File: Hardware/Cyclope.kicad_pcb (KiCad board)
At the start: 2 copper layers, 30 x 80 mm, 75 parts, among them J1 M20-9762042, J2 Motor_2, J3 Motor_1, J4 Front, J5 Front, J8 FTDI, M1 FS5113R, M2 FS5113R, Q1 DMG3414U, Q2 DMG2301L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

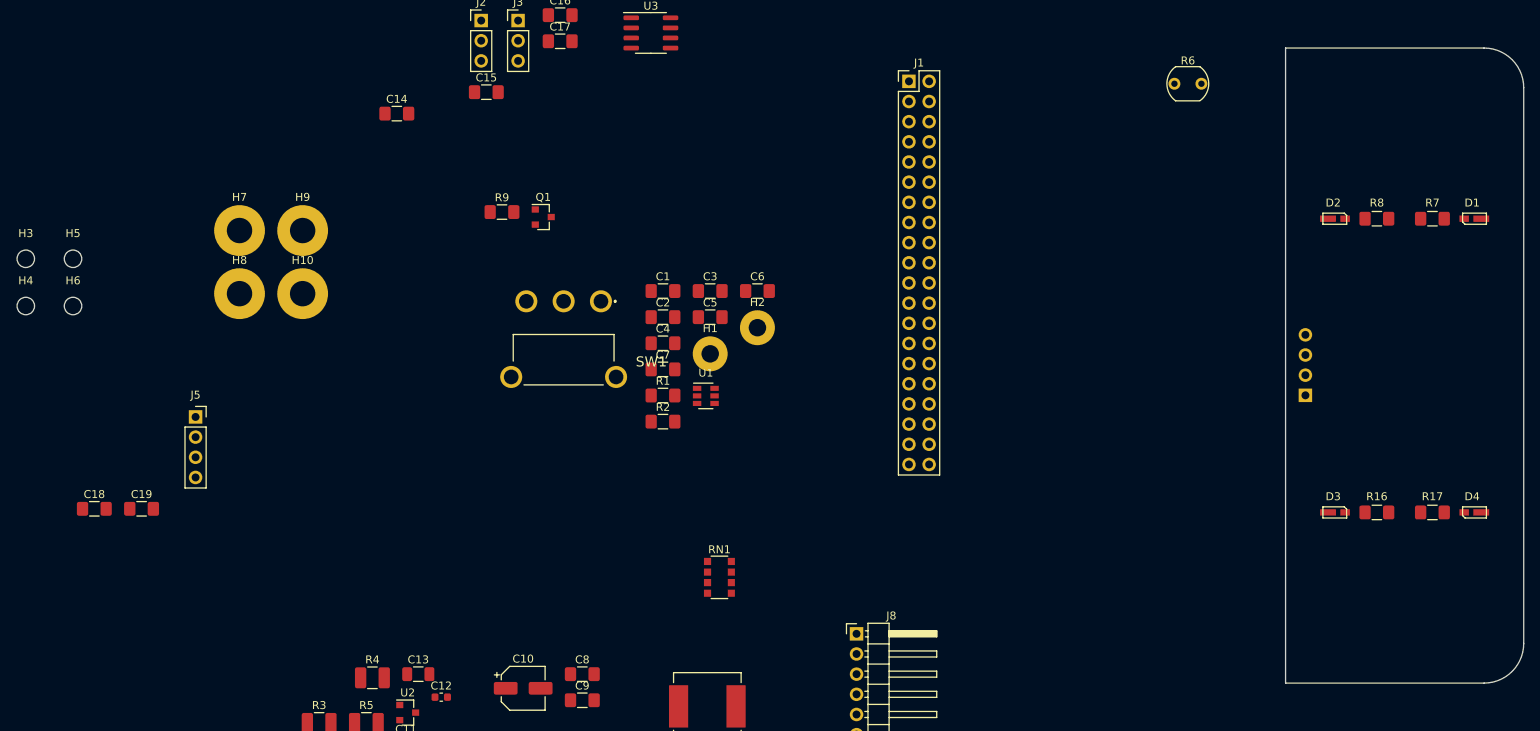
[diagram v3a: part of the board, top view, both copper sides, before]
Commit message: [Hardware] Added camera holes and a cut for camera cable to front board PCB.
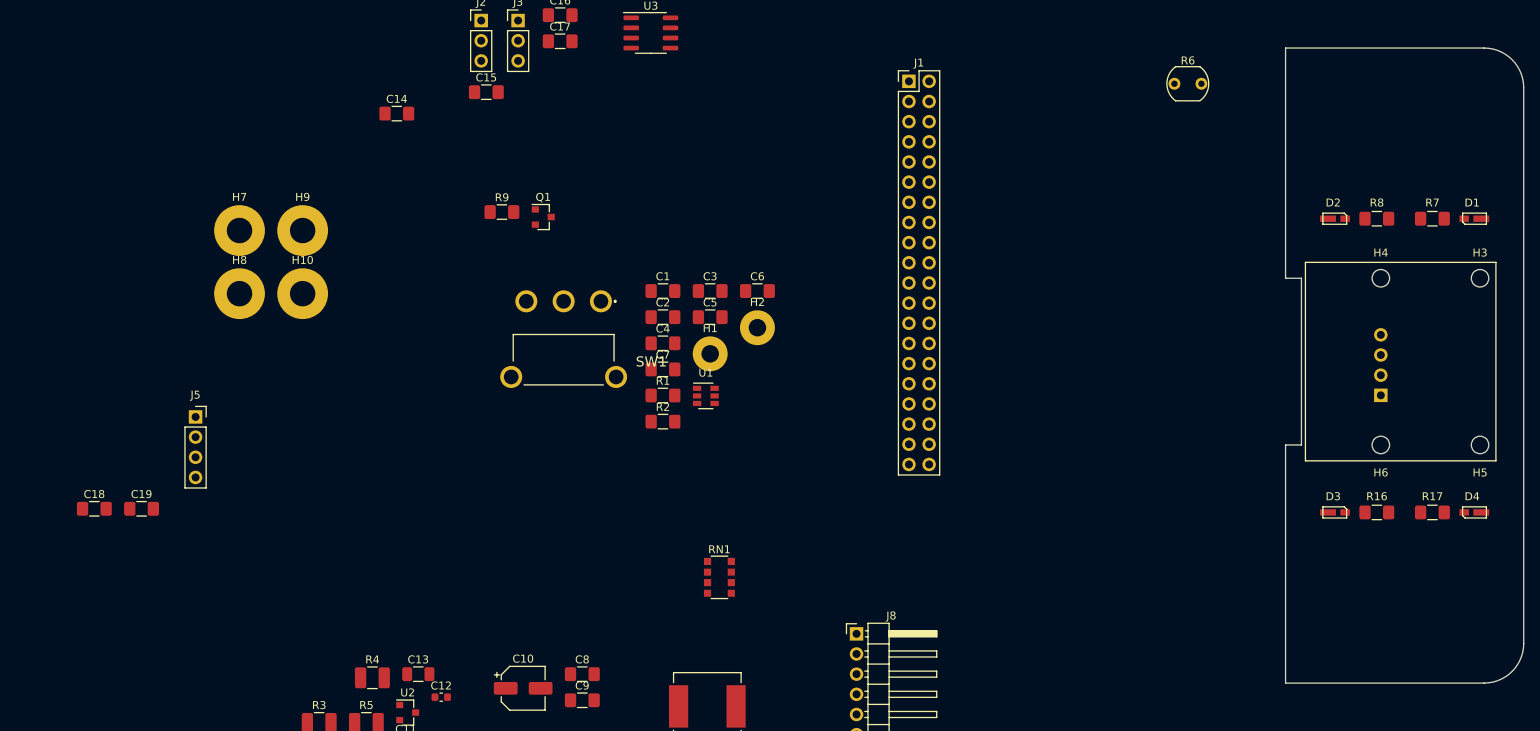
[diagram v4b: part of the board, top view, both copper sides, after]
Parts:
- moved H3 183.2 mm to (234.5, 69.0)
- moved H5 178.8 mm to (234.5, 90.0)
- moved H4 170.7 mm to (222.0, 69.0)
- moved H6 165.7 mm to (222.0, 90.0)
- moved J4 9.50 mm to (222.0, 83.8)
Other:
- outline, holes or cut-outs redrawn
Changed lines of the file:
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@@
   (general
     (thickness 1.6)
-    (drawings 14)
+    (drawings 22)
     (tracks 0)
     (zones 0)
@@
   )
   (module Connector_PinHeader_2.54mm:PinHeader_1x04_P2.54mm_Vertical (layer B.Cu)
-    (at 212.5 83.75)
+    (at 222 83.75)
     (descr "Through hole straight pin header, 1x04, 2.54mm pitch, single row")
     (tags "Through hole pin header THT 1x04 2.54mm single row")
-    (fp_text reference J4 (at 0 2.33) (layer B.SilkS)
+    (fp_text reference J4 (at 0 -10.25) (layer B.SilkS)
       (effects (font (size 1 1) (thickness 0.15)) (justify mirror))
     )
@@
   )
   (module MountingHole:MountingHole_2.2mm_M2 (layer F.Cu)
-    (at 57.258 72.498)
+    (at 222 90)
     (descr "Mounting Hole 2.2mm, no annular, M2")
     (tags "mounting hole 2.2mm no annular m2")
     (attr virtual)
-    (fp_text reference H6 (at 0 -3.2) (layer F.SilkS)
+    (fp_text reference H6 (at 0 3.5) (layer F.SilkS)
       (effects (font (size 1 1) (thickness 0.15)))
     )
@@
   )
   (module MountingHole:MountingHole_2.2mm_M2 (layer F.Cu)
-    (at 57.258 66.548)
+    (at 234.5 90)
     (descr "Mounting Hole 2.2mm, no annular, M2")
     (tags "mounting hole 2.2mm no annular m2")
     (attr virtual)
-    (fp_text reference H5 (at 0 -3.2) (layer F.SilkS)
+    (fp_text reference H5 (at 0 3.5) (layer F.SilkS)
       (effects (font (size 1 1) (thickness 0.15)))
     )
@@
   )
   (module MountingHole:MountingHole_2.2mm_M2 (layer F.Cu)
-    (at 51.308 72.498)
+    (at 222 69)
     (descr "Mounting Hole 2.2mm, no annular, M2")
     (tags "mounting hole 2.2mm no annular m2")
@@
   )
   (module MountingHole:MountingHole_2.2mm_M2 (layer F.Cu)
-    (at 51.308 66.548)
+    (at 234.5 69)
     (descr "Mounting Hole 2.2mm, no annular, M2")
     (tags "mounting hole 2.2mm no annular m2")
@@
     )
   )
-  (dimension 13 (width 0.15) (layer Dwgs.User)
-    (gr_text "13,000 mm" (at 194.2 68 270) (layer Dwgs.User)
-      (effects (font (size 1 1) (thickness 0.15)))
-    )
-    (feature1 (pts (xy 210 74.5) (xy 194.913579 74.5)))
-    (feature2 (pts (xy 210 61.5) (xy 194.913579 61.5)))
-    (crossbar (pts (xy 195.5 61.5) (xy 195.5 74.5)))
-    (arrow1a (pts (xy 195.5 74.5) (xy 194.913579 73.373496)))
-    (arrow1b (pts (xy 195.5 74.5) (xy 196.086421 73.373496)))
-    (arrow2a (pts (xy 195.5 61.5) (xy 194.913579 62.626504)))
-    (arrow2b (pts (xy 195.5 61.5) (xy 196.086421 62.626504)))
-  )
-  (dimension 13 (width 0.15) (layer Dwgs.User)
-    (gr_text "13,000 mm" (at 194.2 92 90) (layer Dwgs.User)
-      (effects (font (size 1 1) (thickness 0.15)))
-    )
-    (feature1 (pts (xy 210 85.5) (xy 194.913579 85.5)))
-    (feature2 (pts (xy 210 98.5) (xy 194.913579 98.5)))
-    (crossbar (pts (xy 195.5 98.5) (xy 195.5 85.5)))
-    (arrow1a (pts (xy 195.5 85.5) (xy 196.086421 86.626504)))
-    (arrow1b (pts (xy 195.5 85.5) (xy 194.913579 86.626504)))
-    (arrow2a (pts (xy 195.5 98.5) (xy 196.086421 97.373496)))
-    (arrow2b (pts (xy 195.5 98.5) (xy 194.913579 97.373496)))
-  )
-  (gr_arc (start 235 45) (end 240 45) (angle -90) (layer Edge.Cuts) (width 0.05))
-  (gr_arc (start 235 115) (end 235 120) (angle -90) (layer Edge.Cuts) (width 0.05))
+  (gr_line (start 210 90) (end 210 120) (layer Edge.Cuts) (width 0.1))
+  (gr_line (start 212 90) (end 210 90) (layer Edge.Cuts) (width 0.05))
+  (gr_line (start 212 69) (end 212 90) (layer Edge.Cuts) (width 0.1))
+  (gr_line (start 210 69) (end 212 69) (layer Edge.Cuts) (width 0.1))
+  (gr_line (start 212.5 92) (end 212.5 67) (layer F.SilkS) (width 0.15))
+  (gr_line (start 236.5 92) (end 212.5 92) (layer F.SilkS) (width 0.15))
+  (gr_line (start 236.5 67) (end 236.5 92) (layer F.SilkS) (width 0.15))
+  (gr_line (start 212.5 67) (end 236.5 67) (layer F.SilkS) (width 0.15))
+  (dimension 12.5 (width 0.15) (layer Dwgs.User)
+    (gr_text "12,500 mm" (at 228.25 129.3) (layer Dwgs.User)
+      (effects (font (size 1 1) (thickness 0.15)))
+    )
+    (feature1 (pts (xy 222 89.5) (xy 222 128.586421)))
+    (feature2 (pts (xy 234.5 89.5) (xy 234.5 128.586421)))
+    (crossbar (pts (xy 234.5 128) (xy 222 128)))
+    (arrow1a (pts (xy 222 128) (xy 223.126504 127.413579)))
+    (arrow1b (pts (xy 222 128) (xy 223.126504 128.586421)))
+    (arrow2a (pts (xy 234.5 128) (xy 233.373496 127.413579)))
+    (arrow2b (pts (xy 234.5 128) (xy 233.373496 128.586421)))
+  )
+  (dimension 21 (width 0.15) (layer Dwgs.User)
+    (gr_text "21,000 mm" (at 248.3 79.5 270) (layer Dwgs.User)
+      (effects (font (size 1 1) (thickness 0.15)))
+    )
+    (feature1 (pts (xy 217.5 90) (xy 247.586421 90)))
+    (feature2 (pts (xy 217.5 69) (xy 247.586421 69)))
+    (crossbar (pts (xy 247 69) (xy 247 90)))
+    (arrow1a (pts (xy 247 90) (xy 246.413579 88.873496)))
+    (arrow1b (pts (xy 247 90) (xy 247.586421 88.873496)))
+    (arrow2a (pts (xy 247 69) (xy 246.413579 70.126504)))
+    (arrow2b (pts (xy 247 69) (xy 247.586421 70.126504)))
+  )
+  (gr_arc (start 235 45) (end 240 45) (angle -90) (layer Edge.Cuts) (width 0.1))
+  (gr_arc (start 235 115) (end 235 120) (angle -90) (layer Edge.Cuts) (width 0.1))
   (dimension 16 (width 0.15) (layer Dwgs.User)
     (gr_text "16,000 mm" (at 252.3 112 270) (layer Dwgs.User)
@@
   (gr_line (start 240 45) (end 240 115) (layer Edge.Cuts) (width 0.1))
   (gr_line (start 210 40) (end 235 40) (layer Edge.Cuts) (width 0.1))
-  (gr_line (start 210 120) (end 210 40) (layer Edge.Cuts) (width 0.1))
+  (gr_line (start 210 69) (end 210 40) (layer Edge.Cuts) (width 0.1))
   (gr_line (start 235 120) (end 210 120) (layer Edge.Cuts) (width 0.1))
   (gr_text GND (at 169.164 113.792) (layer F.Mask)

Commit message: [Hardware] Positionned LDR on front board PCB.
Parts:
- moved R6 82.8 mm to (236.0, 117.0), turned to 90 degrees
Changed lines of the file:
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@@
   )
   (module OptoDevice:R_LDR_5.1x4.3mm_P3.4mm_Vertical (layer F.Cu)
-    (at 196 44.5)
+    (at 236 117 90)
     (descr "Resistor, LDR 5.1x3.4mm, see http://yourduino.com/docs/Photoresistor-5516-datasheet.pdf")
     (tags "Resistor LDR5.1x3.4mm")
-    (fp_text reference R6 (at 1.7 -2.9) (layer F.SilkS)
+    (fp_text reference R6 (at 5.5 0 180) (layer F.SilkS)
       (effects (font (size 1 1) (thickness 0.15)))
     )
-    (fp_text value LDR07 (at 1.5 3) (layer F.Fab) hide
+    (fp_text value LDR07 (at 1.5 3 90) (layer F.Fab) hide
       (effects (font (size 1 1) (thickness 0.15)))
     )
@@
     (fp_line (start 0.15 -2.15) (end 3.2 -2.15) (layer F.SilkS) (width 0.12))
     (fp_line (start 0.15 2.15) (end 3.2 2.15) (layer F.SilkS) (width 0.12))
-    (fp_text user %R (at 1.7 -2.9) (layer F.Fab)
+    (fp_text user %R (at 5.5 0 180) (layer F.Fab)
       (effects (font (size 1 1) (thickness 0.15)))
     )
-    (pad 2 thru_hole circle (at 3.4 0) (size 1.5 1.5) (drill 0.8) (layers *.Cu *.Mask)
+    (pad 2 thru_hole circle (at 3.4 0 90) (size 1.5 1.5) (drill 0.8) (layers *.Cu *.Mask)
       (net 45 GNDD))
-    (pad 1 thru_hole circle (at 0 0) (size 1.5 1.5) (drill 0.8) (layers *.Cu *.Mask)
+    (pad 1 thru_hole circle (at 0 0 90) (size 1.5 1.5) (drill 0.8) (layers *.Cu *.Mask)
       (net 59 "Net-(J4-Pad2)"))
     (model ${KISYS3DMOD}/OptoDevice.3dshapes/R_LDR_5.1x4.3mm_P3.4mm_Vertical.wrl

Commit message: [Hardware] Increased front board PCB size to match chassis dimensions.
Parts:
- moved R6 9.00 mm to (236.0, 126.0)
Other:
- board size 30 x 80 mm -> 30 x 100 mm
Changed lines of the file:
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@@
   )
   (module OptoDevice:R_LDR_5.1x4.3mm_P3.4mm_Vertical (layer F.Cu)
-    (at 236 117 90)
+    (at 236 126 90)
     (descr "Resistor, LDR 5.1x3.4mm, see http://yourduino.com/docs/Photoresistor-5516-datasheet.pdf")
     (tags "Resistor LDR5.1x3.4mm")
@@
     )
   )
-  (gr_line (start 210 90) (end 210 120) (layer Edge.Cuts) (width 0.1))
+  (gr_line (start 210 90) (end 210 130) (layer Edge.Cuts) (width 0.1))
   (gr_line (start 212 90) (end 210 90) (layer Edge.Cuts) (width 0.05))
   (gr_line (start 212 69) (end 212 90) (layer Edge.Cuts) (width 0.1))
@@
     (arrow2b (pts (xy 247 69) (xy 247.586421 70.126504)))
   )
-  (gr_arc (start 235 45) (end 240 45) (angle -90) (layer Edge.Cuts) (width 0.1))
-  (gr_arc (start 235 115) (end 235 120) (angle -90) (layer Edge.Cuts) (width 0.1))
+  (gr_arc (start 235 35) (end 240 35) (angle -90) (layer Edge.Cuts) (width 0.1))
+  (gr_arc (start 235 125) (end 235 130) (angle -90) (layer Edge.Cuts) (width 0.1))
   (dimension 16 (width 0.15) (layer Dwgs.User)
     (gr_text "16,000 mm" (at 252.3 112 270) (layer Dwgs.User)
@@
     (arrow2b (pts (xy 251 40) (xy 251.586421 41.126504)))
   )
-  (gr_line (start 240 45) (end 240 115) (layer Edge.Cuts) (width 0.1))
-  (gr_line (start 210 40) (end 235 40) (layer Edge.Cuts) (width 0.1))
-  (gr_line (start 210 69) (end 210 40) (layer Edge.Cuts) (width 0.1))
-  (gr_line (start 235 120) (end 210 120) (layer Edge.Cuts) (width 0.1))
+  (gr_line (start 240 35) (end 240 125) (layer Edge.Cuts) (width 0.1))
+  (gr_line (start 210 30) (end 235 30) (layer Edge.Cuts) (width 0.1))
+  (gr_line (start 210 69) (end 210 30) (layer Edge.Cuts) (width 0.1))
+  (gr_line (start 235 130) (end 210 130) (layer Edge.Cuts) (width 0.1))
   (gr_text GND (at 169.164 113.792) (layer F.Mask)
     (effects (font (size 1 1) (thickness 0.15)))
